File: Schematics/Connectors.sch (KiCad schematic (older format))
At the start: 101 parts, among them P601 CONN_02X05, P602 CONN_02X05, P603 CONN_02X05, P604 CONN_02X05, P605 CONN_02X05, P606 CONN_6X2, P607 CONN_02X05, P608 CONN_02X05, P609 CONN_02X20, P610 CONN_02X05, P611 CONN_02X05, P612 CONN_02X05, P613 CONN_02X05, P614 CONN_02X05, P615 CONN_02X05, P616 CONN_02X05

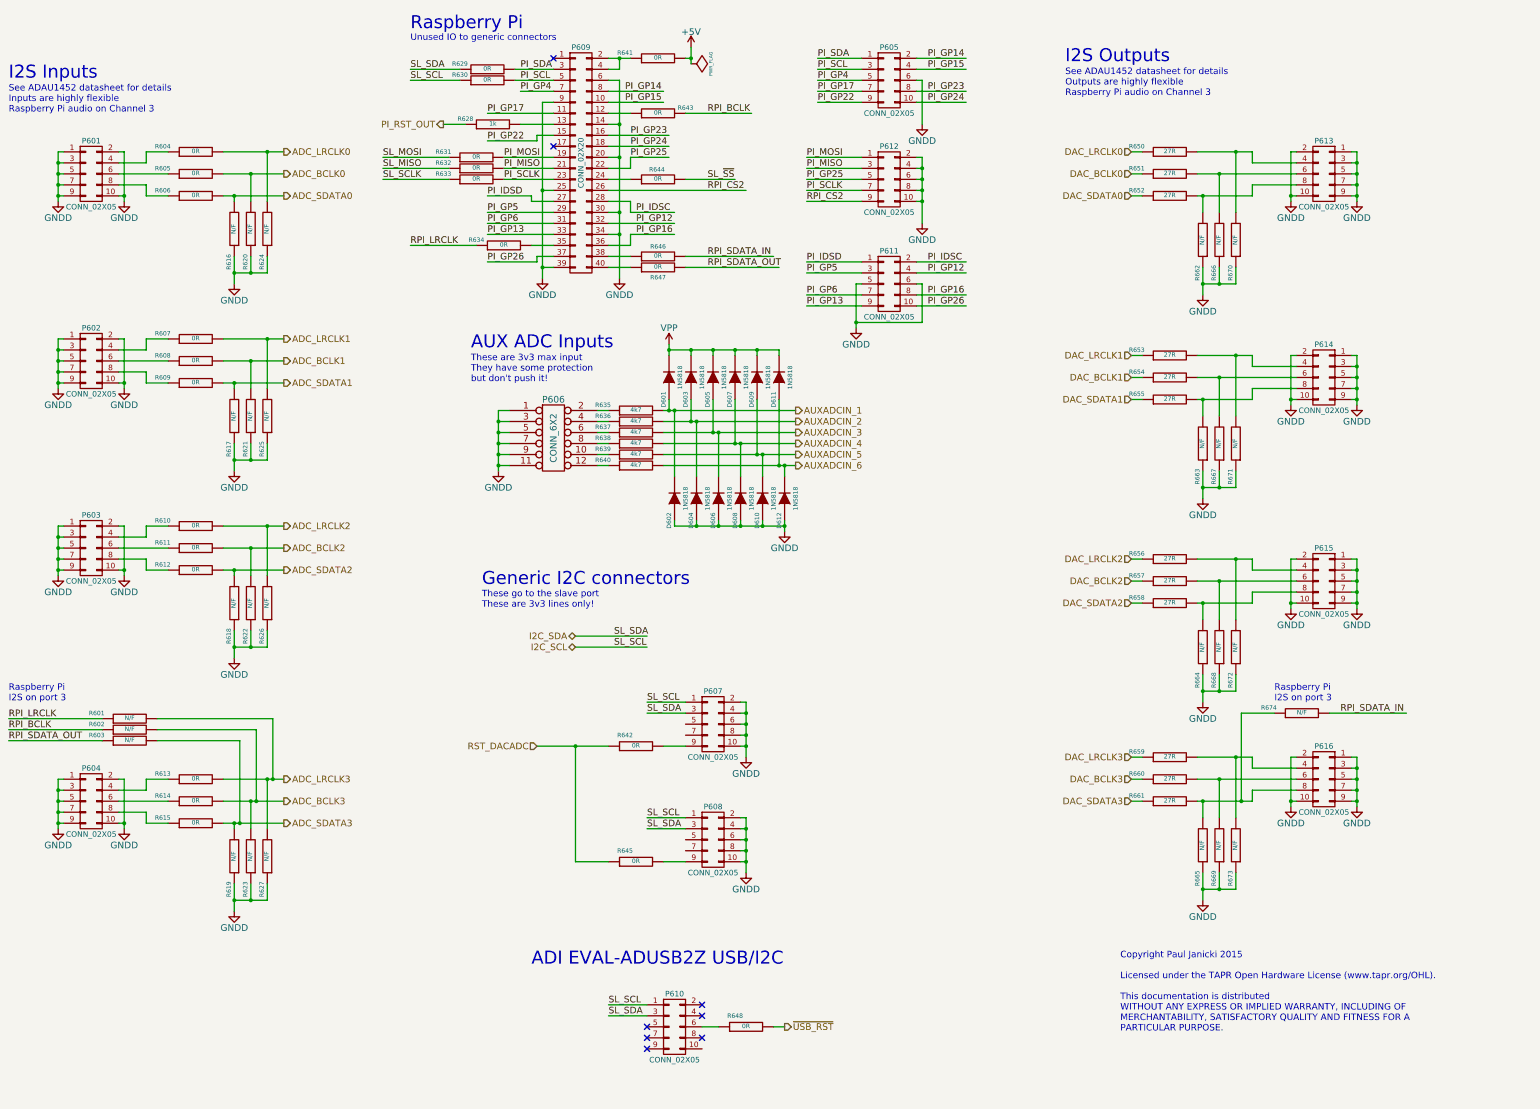
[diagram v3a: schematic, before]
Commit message: WIP
Add master audio clock to I2S headers.
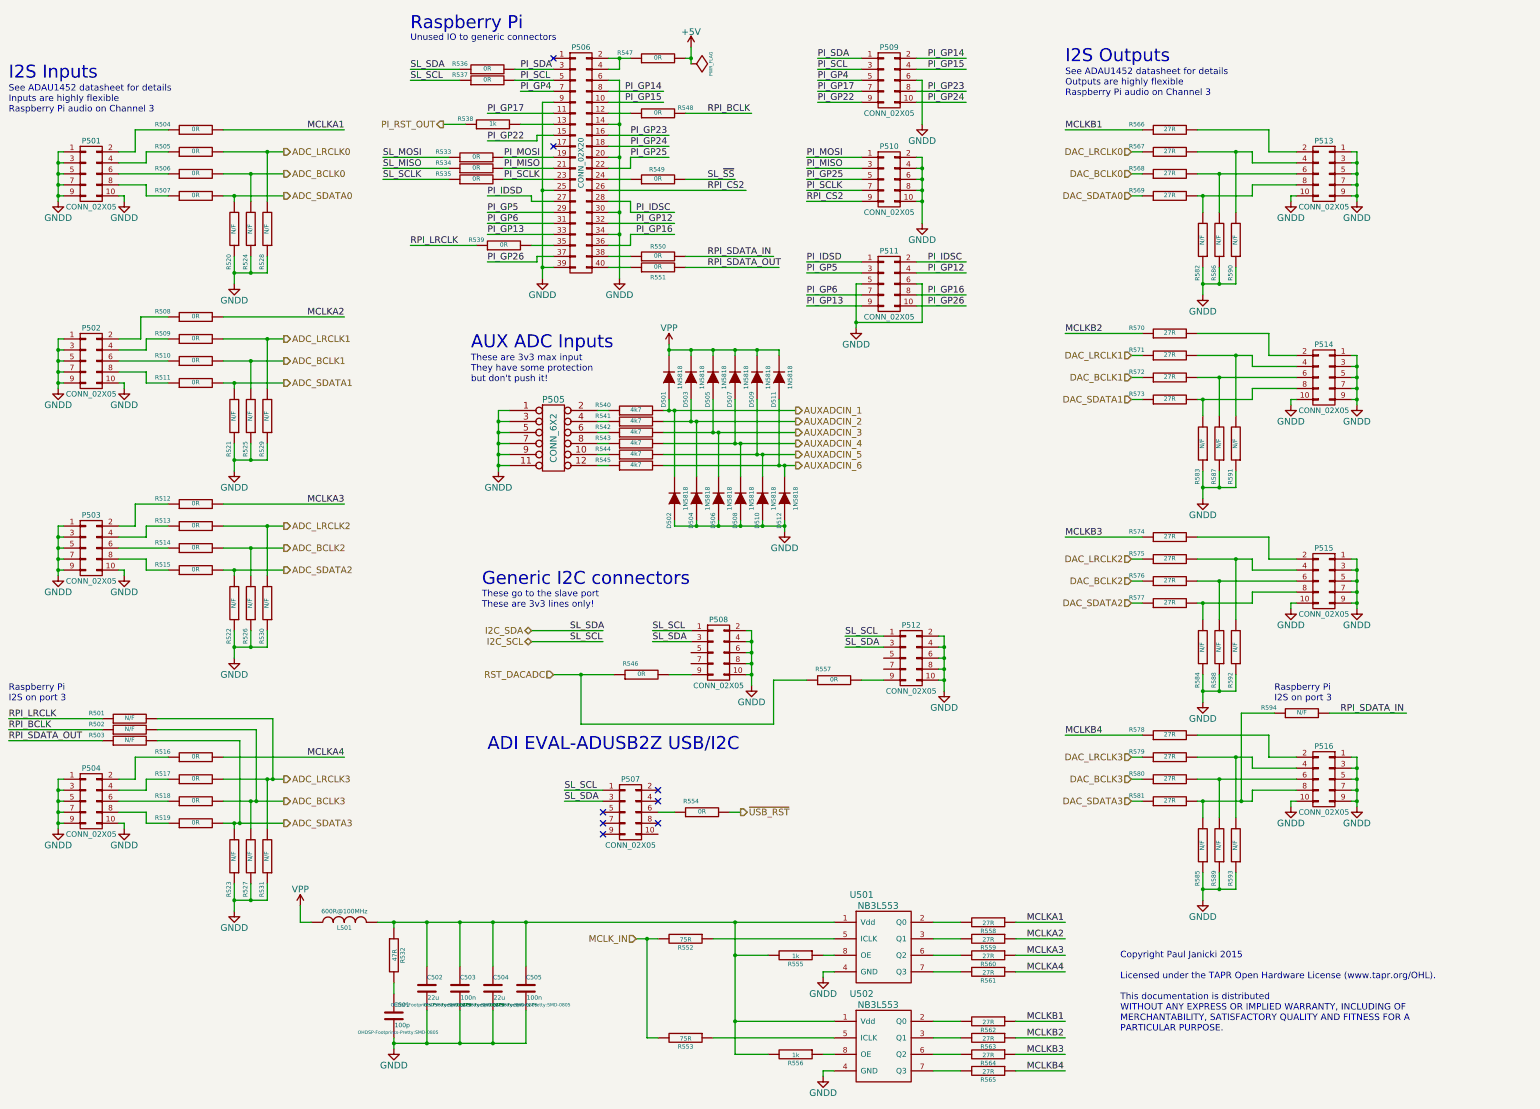
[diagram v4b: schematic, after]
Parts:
- added C501: 100p, OHDSP-Footprints-Pretty:SMD-0805, symbol C
- added C502, C504: 22u, OHDSP-Footprints-Pretty:SMD-0805, symbol C
- added C503, C505: 100n, OHDSP-Footprints-Pretty:SMD-0805, symbol C
- added L501: 600R@100MHz, OHDSP-Footprints-Pretty:SMD-0805, symbol INDUCTOR
- added R504, R508, R512, R516: 0R, OHDSP-Footprints-Pretty:SMD-0805, symbol R
- added R532: 47R, OHDSP-Footprints-Pretty:SMD-0805, symbol R
- added R552, R553: 75R, OHDSP-Footprints-Pretty:SMD-0805, symbol R
- added R555, R556: 1k, OHDSP-Footprints-Pretty:SMD-0805, symbol R
- added R558, R559, R560, R561, R562, R563, R564, R565, R566, R570, R574, R578: 27R, OHDSP-Footprints-Pretty:SMD-0805, symbol R
- added U501, U502: NB3L553, OHDSP-Footprints-Pretty:IC_SOIC_8, symbol IC-CLK-FANOUT-NB3L553
- R505: renamed from R604; footprint OHDSP-Footprints-Pretty:SMD-0603 -> OHDSP-Footprints-Pretty:SMD-0805
- R506: renamed from R605; footprint OHDSP-Footprints-Pretty:SMD-0603 -> OHDSP-Footprints-Pretty:SMD-0805
- R507: renamed from R606; footprint OHDSP-Footprints-Pretty:SMD-0603 -> OHDSP-Footprints-Pretty:SMD-0805
- R509: renamed from R607; footprint OHDSP-Footprints-Pretty:SMD-0603 -> OHDSP-Footprints-Pretty:SMD-0805
- R510: renamed from R608; footprint OHDSP-Footprints-Pretty:SMD-0603 -> OHDSP-Footprints-Pretty:SMD-0805
- R511: renamed from R609; footprint OHDSP-Footprints-Pretty:SMD-0603 -> OHDSP-Footprints-Pretty:SMD-0805
- R513: renamed from R610; footprint OHDSP-Footprints-Pretty:SMD-0603 -> OHDSP-Footprints-Pretty:SMD-0805
- R514: renamed from R611; footprint OHDSP-Footprints-Pretty:SMD-0603 -> OHDSP-Footprints-Pretty:SMD-0805
- R515: renamed from R612; footprint OHDSP-Footprints-Pretty:SMD-0603 -> OHDSP-Footprints-Pretty:SMD-0805
- R517: renamed from R613; footprint OHDSP-Footprints-Pretty:SMD-0603 -> OHDSP-Footprints-Pretty:SMD-0805
- R518: renamed from R614; footprint OHDSP-Footprints-Pretty:SMD-0603 -> OHDSP-Footprints-Pretty:SMD-0805
- R519: renamed from R615; footprint OHDSP-Footprints-Pretty:SMD-0603 -> OHDSP-Footprints-Pretty:SMD-0805
- R520: renamed from R616; footprint OHDSP-Footprints-Pretty:SMD-0603 -> OHDSP-Footprints-Pretty:SMD-0805
- R521: renamed from R617; footprint OHDSP-Footprints-Pretty:SMD-0603 -> OHDSP-Footprints-Pretty:SMD-0805
- R522: renamed from R618; footprint OHDSP-Footprints-Pretty:SMD-0603 -> OHDSP-Footprints-Pretty:SMD-0805
- R523: renamed from R619; footprint OHDSP-Footprints-Pretty:SMD-0603 -> OHDSP-Footprints-Pretty:SMD-0805
- R524: renamed from R620; footprint OHDSP-Footprints-Pretty:SMD-0603 -> OHDSP-Footprints-Pretty:SMD-0805
- R525: renamed from R621; footprint OHDSP-Footprints-Pretty:SMD-0603 -> OHDSP-Footprints-Pretty:SMD-0805
- R526: renamed from R622; footprint OHDSP-Footprints-Pretty:SMD-0603 -> OHDSP-Footprints-Pretty:SMD-0805
- R527: renamed from R623; footprint OHDSP-Footprints-Pretty:SMD-0603 -> OHDSP-Footprints-Pretty:SMD-0805
- R528: renamed from R624; footprint OHDSP-Footprints-Pretty:SMD-0603 -> OHDSP-Footprints-Pretty:SMD-0805
- R529: renamed from R625; footprint OHDSP-Footprints-Pretty:SMD-0603 -> OHDSP-Footprints-Pretty:SMD-0805
- R530: renamed from R626; footprint OHDSP-Footprints-Pretty:SMD-0603 -> OHDSP-Footprints-Pretty:SMD-0805
- R531: renamed from R627; footprint OHDSP-Footprints-Pretty:SMD-0603 -> OHDSP-Footprints-Pretty:SMD-0805
- R567: renamed from R650; footprint OHDSP-Footprints-Pretty:SMD-0603 -> OHDSP-Footprints-Pretty:SMD-0805
- R568: renamed from R651; footprint OHDSP-Footprints-Pretty:SMD-0603 -> OHDSP-Footprints-Pretty:SMD-0805
- R569: renamed from R652; footprint OHDSP-Footprints-Pretty:SMD-0603 -> OHDSP-Footprints-Pretty:SMD-0805
- R571: renamed from R653; footprint OHDSP-Footprints-Pretty:SMD-0603 -> OHDSP-Footprints-Pretty:SMD-0805
- R572: renamed from R654; footprint OHDSP-Footprints-Pretty:SMD-0603 -> OHDSP-Footprints-Pretty:SMD-0805
- R573: renamed from R655; footprint OHDSP-Footprints-Pretty:SMD-0603 -> OHDSP-Footprints-Pretty:SMD-0805
- R575: renamed from R656; footprint OHDSP-Footprints-Pretty:SMD-0603 -> OHDSP-Footprints-Pretty:SMD-0805
- R576: renamed from R657; footprint OHDSP-Footprints-Pretty:SMD-0603 -> OHDSP-Footprints-Pretty:SMD-0805
- R577: renamed from R658; footprint OHDSP-Footprints-Pretty:SMD-0603 -> OHDSP-Footprints-Pretty:SMD-0805
- R579: renamed from R659; footprint OHDSP-Footprints-Pretty:SMD-0603 -> OHDSP-Footprints-Pretty:SMD-0805
- R580: renamed from R660; footprint OHDSP-Footprints-Pretty:SMD-0603 -> OHDSP-Footprints-Pretty:SMD-0805
- R581: renamed from R661; footprint OHDSP-Footprints-Pretty:SMD-0603 -> OHDSP-Footprints-Pretty:SMD-0805
- R582: renamed from R662; footprint OHDSP-Footprints-Pretty:SMD-0603 -> OHDSP-Footprints-Pretty:SMD-0805
- R583: renamed from R663; footprint OHDSP-Footprints-Pretty:SMD-0603 -> OHDSP-Footprints-Pretty:SMD-0805
- R584: renamed from R664; footprint OHDSP-Footprints-Pretty:SMD-0603 -> OHDSP-Footprints-Pretty:SMD-0805
- R585: renamed from R665; footprint OHDSP-Footprints-Pretty:SMD-0603 -> OHDSP-Footprints-Pretty:SMD-0805
- R586: renamed from R666; footprint OHDSP-Footprints-Pretty:SMD-0603 -> OHDSP-Footprints-Pretty:SMD-0805
- R587: renamed from R667; footprint OHDSP-Footprints-Pretty:SMD-0603 -> OHDSP-Footprints-Pretty:SMD-0805
- R588: renamed from R668; footprint OHDSP-Footprints-Pretty:SMD-0603 -> OHDSP-Footprints-Pretty:SMD-0805
- R589: renamed from R669; footprint OHDSP-Footprints-Pretty:SMD-0603 -> OHDSP-Footprints-Pretty:SMD-0805
- R590: renamed from R670; footprint OHDSP-Footprints-Pretty:SMD-0603 -> OHDSP-Footprints-Pretty:SMD-0805
- R591: renamed from R671; footprint OHDSP-Footprints-Pretty:SMD-0603 -> OHDSP-Footprints-Pretty:SMD-0805
- R592: renamed from R672; footprint OHDSP-Footprints-Pretty:SMD-0603 -> OHDSP-Footprints-Pretty:SMD-0805
- R593: renamed from R673; footprint OHDSP-Footprints-Pretty:SMD-0603 -> OHDSP-Footprints-Pretty:SMD-0805
- renumbered D601 to D501, D602 to D502, D603 to D503, D604 to D504, D605 to D505, D606 to D506, D607 to D507, D608 to D508, D609 to D509, D610 to D510, D611 to D511, D612 to D512, P601 to P501, P602 to P502, P603 to P503, P604 to P504, P606 to P505, P609 to P506, P610 to P507, P607 to P508, P605 to P509, P612 to P510, P611 to P511, P608 to P512, P613 to P513, P614 to P514, P615 to P515, P616 to P516, R601 to R501, R602 to R502, R603 to R503, R631 to R533, R632 to R534, R633 to R535, R629 to R536, R630 to R537, R628 to R538, R634 to R539, R635 to R540, R636 to R541, R637 to R542, R638 to R543, R639 to R544, R640 to R545, R642 to R546, R641 to R547, R643 to R548, R644 to R549, R646 to R550, R647 to R551, R648 to R554, R645 to R557, R674 to R594
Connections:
- net labels added: MCLKA1, MCLKA2, MCLKA3, MCLKA4, MCLKB1, MCLKB2, MCLKB3, MCLKB4, MCLK_IN
- wire segments 393 -> 465
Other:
- moved on the sheet: P507, P508, P512, R546, R554, R557

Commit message: WIP
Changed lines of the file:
@@
 Text Label 11000 10900 0    60   ~ 0
 MCLKB4
+Text Label 4800 4050 2    60   ~ 0
+MCLKA1
 Text Label 4800 2350 2    60   ~ 0
-MCLKA1
-Text Label 4800 4050 2    60   ~ 0
 MCLKA2
 Text Label 4800 5750 2    60   ~ 0

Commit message: WIP
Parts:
- removed P508, P512: CONN_02X05, OHDSP-Footprints-Pretty:CONN_DIL_2X5, symbol CONN_02X05
- added P508, P512: CONN_4x1, OHDSP-Footprints-Pretty:CONN_SIL_4, symbol CONN_4x1
- P507: footprint OHDSP-Footprints-Pretty:CONN_DIL_2X5 -> OHDSP-Footprints-Pretty:CONN_DIL_2X5_BOX
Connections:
- wire segments 465 -> 457
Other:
- moved on the sheet: R546, R557
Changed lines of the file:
@@
 	1    0    0    -1
 $EndComp
-$Comp
-L CONN_02X05 P507
-U 1 1 54DC056C
-P 7400 8550
-F 0 "P507" H 7400 8850 50  0000 C CNN
-F 1 "CONN_02X05" H 7400 8250 50  0000 C CNN
-F 2 "OHDSP-Footprints-Pretty:CONN_DIL_2X5" H 7400 7350 60  0001 C CNN
-F 3 "" H 7400 7350 60  0000 C CNN
-	1    7400 8550
-	1    0    0    -1
-$EndComp
 Text Notes 6100 8000 0    118  ~ 0
 ADI EVAL-ADUSB2Z USB/I2C
@@
 L GNDD #PWR091
 U 1 1 54DC2149
-P 8500 7400
-F 0 "#PWR091" H 8500 7150 60  0001 C CNN
-F 1 "GNDD" H 8500 7250 60  0000 C CNN
-F 2 "" H 8500 7400 60  0000 C CNN
-F 3 "" H 8500 7400 60  0000 C CNN
-	1    8500 7400
+P 7850 7400
+F 0 "#PWR091" H 7850 7150 60  0001 C CNN
+F 1 "GNDD" H 7850 7250 60  0000 C CNN
+F 2 "" H 7850 7400 60  0000 C CNN
+F 3 "" H 7850 7400 60  0000 C CNN
+	1    7850 7400
 	1    0    0    -1
 $EndComp
@@
 $EndComp
 $Comp
-L CONN_02X05 P508
-U 1 1 54E480C2
-P 8200 7100
-F 0 "P508" H 8200 7400 50  0000 C CNN
-F 1 "CONN_02X05" H 8200 6800 50  0000 C CNN
-F 2 "OHDSP-Footprints-Pretty:CONN_DIL_2X5" H 8200 5900 60  0001 C CNN
-F 3 "" H 8200 5900 60  0000 C CNN
-	1    8200 7100
-	1    0    0    -1
-$EndComp
-$Comp
 L R R538
 U 1 1 54E4AF9E
@@
 $EndComp
 $Comp
-L CONN_02X05 P512
-U 1 1 54E55D44
-P 9950 7150
-F 0 "P512" H 9950 7450 50  0000 C CNN
-F 1 "CONN_02X05" H 9950 6850 50  0000 C CNN
-F 2 "OHDSP-Footprints-Pretty:CONN_DIL_2X5" H 9950 5950 60  0001 C CNN
-F 3 "" H 9950 5950 60  0000 C CNN
-	1    9950 7150
-	1    0    0    -1
-$EndComp
-$Comp
 L DIODE D501
 U 1 1 54E4E268
@@
 Text Label 7600 7000 0    60   ~ 0
 SL_SDA
-Text Label 9350 6950 0    60   ~ 0
-SL_SCL
-Text Label 9350 7050 0    60   ~ 0
-SL_SDA
-$Comp
-L GNDD #PWR0124
-U 1 1 551A75F1
-P 10250 7450
-F 0 "#PWR0124" H 10250 7200 60  0001 C CNN
-F 1 "GNDD" H 10250 7300 60  0000 C CNN
-F 2 "" H 10250 7450 60  0000 C CNN
-F 3 "" H 10250 7450 60  0000 C CNN
-	1    10250 7450
-	1    0    0    -1
-$EndComp
 $Comp
 L R R546
 U 1 1 551A97CD
-P 7500 7300
-F 0 "R546" V 7600 7400 40  0000 C CNN
-F 1 "0R" V 7507 7301 40  0000 C CNN
-F 2 "OHDSP-Footprints-Pretty:SMD-0805" V 7430 7300 30  0001 C CNN
-F 3 "~" H 7500 7300 30  0000 C CNN
-	1    7500 7300
+P 7500 7200
+F 0 "R546" V 7600 7300 40  0000 C CNN
+F 1 "0R" V 7507 7201 40  0000 C CNN
+F 2 "OHDSP-Footprints-Pretty:SMD-0805" V 7430 7200 30  0001 C CNN
+F 3 "~" H 7500 7200 30  0000 C CNN
+	1    7500 7200
 	0    -1   -1   0
 $EndComp
-Text HLabel 6700 7300 0    60   Input ~ 0
+Text HLabel 6700 7200 0    60   Input ~ 0
 RST_DACADC
 $Comp
 L R R557
 U 1 1 551B7A65
-P 9250 7350
-F 0 "R557" V 9350 7450 40  0000 C CNN
-F 1 "0R" V 9257 7351 40  0000 C CNN
-F 2 "OHDSP-Footprints-Pretty:SMD-0805" V 9180 7350 30  0001 C CNN
-F 3 "~" H 9250 7350 30  0000 C CNN
-	1    9250 7350
+P 9050 7250
+F 0 "R557" V 9150 7350 40  0000 C CNN
+F 1 "0R" V 9057 7251 40  0000 C CNN
+F 2 "OHDSP-Footprints-Pretty:SMD-0805" V 8980 7250 30  0001 C CNN
+F 3 "~" H 9050 7250 30  0000 C CNN
+	1    9050 7250
 	0    -1   -1   0
 $EndComp
@@
 $EndComp
 $Comp
-L GNDD #PWR0125
+L GNDD #PWR0124
 U 1 1 55623365
 P 9150 10050
-F 0 "#PWR0125" H 9150 9800 60  0001 C CNN
+F 0 "#PWR0124" H 9150 9800 60  0001 C CNN
 F 1 "GNDD" H 9150 9900 60  0000 C CNN
 F 2 "" H 9150 10050 60  0000 C CNN
@@
 $EndComp
 $Comp
-L GNDD #PWR0126
+L GNDD #PWR0125
 U 1 1 5562338E
 P 5250 10700
-F 0 "#PWR0126" H 5250 10450 60  0001 C CNN
+F 0 "#PWR0125" H 5250 10450 60  0001 C CNN
 F 1 "GNDD" H 5250 10550 60  0000 C CNN
 F 2 "" H 5250 10700 60  0000 C CNN
@@
 $EndComp
 $Comp
-L VPP #PWR0127
+L VPP #PWR0126
 U 1 1 556233B2
 P 4400 9400
-F 0 "#PWR0127" H 4400 9250 60  0001 C CNN
+F 0 "#PWR0126" H 4400 9250 60  0001 C CNN
 F 1 "VPP" H 4400 9550 60  0000 C CNN
 F 2 "" H 4400 9400 60  0000 C CNN
@@
 $EndComp
 $Comp
-L GNDD #PWR0128
+L GNDD #PWR0127
 U 1 1 5562ABC4
 P 9150 10950
-F 0 "#PWR0128" H 9150 10700 60  0001 C CNN
+F 0 "#PWR0127" H 9150 10700 60  0001 C CNN
 F 1 "GNDD" H 9150 10800 60  0000 C CNN
 F 2 "" H 9150 10950 60  0000 C CNN
@@
 $EndComp
 $Comp
-L GNDD #PWR0129
+L GNDD #PWR0128
 U 1 1 54E3DFB4
 P 13400 6700
-F 0 "#PWR0129" H 13400 6450 60  0001 C CNN
+F 0 "#PWR0128" H 13400 6450 60  0001 C CNN
 F 1 "GNDD" H 13400 6550 60  0000 C CNN
 F 2 "" H 13400 6700 60  0000 C CNN
@@
 Wire Wire Line
 	6800 8350 7150 8350
-Wire Wire Line
-	8500 7300 8450 7300
-Wire Wire Line
-	8500 6900 8500 7400
 Connection ~ 6200 5000
 Wire Wire Line
@@
 	7600 6900 7950 6900
 Wire Wire Line
-	9350 7050 9700 7050
-Wire Wire Line
-	9350 6950 9700 6950
-Wire Wire Line
-	10250 7350 10200 7350
-Wire Wire Line
-	10250 6950 10250 7450
-Wire Wire Line
-	10200 6950 10250 6950
-Connection ~ 10250 7350
-Wire Wire Line
-	10200 7050 10250 7050
-Connection ~ 10250 7050
-Wire Wire Line
-	10200 7250 10250 7250
-Connection ~ 10250 7250
-Wire Wire Line
-	8450 7200 8500 7200
-Connection ~ 8500 7300
+	6700 7200 7250 7200
 Wire Wire Line
-	8450 7000 8500 7000
-Connection ~ 8500 7200
+	8800 7250 8700 7250
+Connection ~ 6950 7200
 Wire Wire Line
-	8450 6900 8500 6900
-Connection ~ 8500 7000
-Wire Wire Line
-	7750 7300 7950 7300
-Wire Wire Line
-	6700 7300 7250 7300
-Wire Wire Line
-	8450 7100 8500 7100
-Connection ~ 8500 7100
-Wire Wire Line
-	10200 7150 10250 7150
-Connection ~ 10250 7150
-Wire Wire Line
-	9500 7350 9700 7350
-Wire Wire Line
-	9000 7350 8700 7350
-Connection ~ 6950 7300
-Wire Wire Line
-	6950 7300 6950 7750
+	6950 7200 6950 7750
 Wire Wire Line
 	6950 7750 8700 7750
 Wire Wire Line
-	8700 7750 8700 7350
+	8700 7750 8700 7250
 Wire Wire Line
 	8150 9700 9250 9700
@@
 Connection ~ 8350 9550
 Wire Wire Line
-	7650 9700 7450 9700
+	7450 9700 7650 9700
 Wire Wire Line
 	6150 10650 6150 10350
@@
 	6150 9550 6150 9950
 Wire Wire Line
-	8350 10750 8350 9550
+	8350 9550 8350 10750
+$Comp
+L CONN_02X05 P507
+U 1 1 54DC056C
+P 7400 8550
+F 0 "P507" H 7400 8850 50  0000 C CNN
+F 1 "CONN_02X05" H 7400 8250 50  0000 C CNN
+F 2 "OHDSP-Footprints-Pretty:CONN_DIL_2X5_BOX" H 7400 7350 60  0001 C CNN
+F 3 "" H 7400 7350 60  0000 C CNN
+	1    7400 8550
+	1    0    0    -1
+$EndComp
+$Comp
+L CONN_4x1 P508
+U 1 1 556C65A2
+P 7950 6900
+F 0 "P508" V 8435 6595 40  0000 C CNN
+F 1 "CONN_4x1" V 8380 6710 40  0000 C CNN
+F 2 "OHDSP-Footprints-Pretty:CONN_SIL_4" H 8290 6790 60  0001 C CNN
+F 3 "" H 8290 6790 60  0000 C CNN
+	1    7950 6900
+	1    0    0    -1
+$EndComp
+Wire Wire Line
+	7950 7100 7850 7100
+Wire Wire Line
+	7850 7100 7850 7400
+Wire Wire Line
+	7750 7200 7950 7200
+$Comp
+L GNDD #PWR0129
+U 1 1 556C820A
+P 9400 7450
+F 0 "#PWR0129" H 9400 7200 60  0001 C CNN
+F 1 "GNDD" H 9400 7300 60  0000 C CNN
+F 2 "" H 9400 7450 60  0000 C CNN
+F 3 "" H 9400 7450 60  0000 C CNN
+	1    9400 7450
+	1    0    0    -1
+$EndComp
+Text Label 9150 6950 0    60   ~ 0
+SL_SCL
+Text Label 9150 7050 0    60   ~ 0
+SL_SDA
+Wire Wire Line
+	9150 7050 9500 7050
+Wire Wire Line
+	9150 6950 9500 6950
+$Comp
+L CONN_4x1 P512
+U 1 1 556C821A
+P 9500 6950
+F 0 "P512" V 9985 6645 40  0000 C CNN
+F 1 "CONN_4x1" V 9930 6760 40  0000 C CNN
+F 2 "OHDSP-Footprints-Pretty:CONN_SIL_4" H 9840 6840 60  0001 C CNN
+F 3 "" H 9840 6840 60  0000 C CNN
+	1    9500 6950
+	1    0    0    -1
+$EndComp
+Wire Wire Line
+	9500 7150 9400 7150
+Wire Wire Line
+	9400 7150 9400 7450
+Wire Wire Line
+	9300 7250 9500 7250
 $EndSCHEMATC
